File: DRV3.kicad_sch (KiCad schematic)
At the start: 15 parts

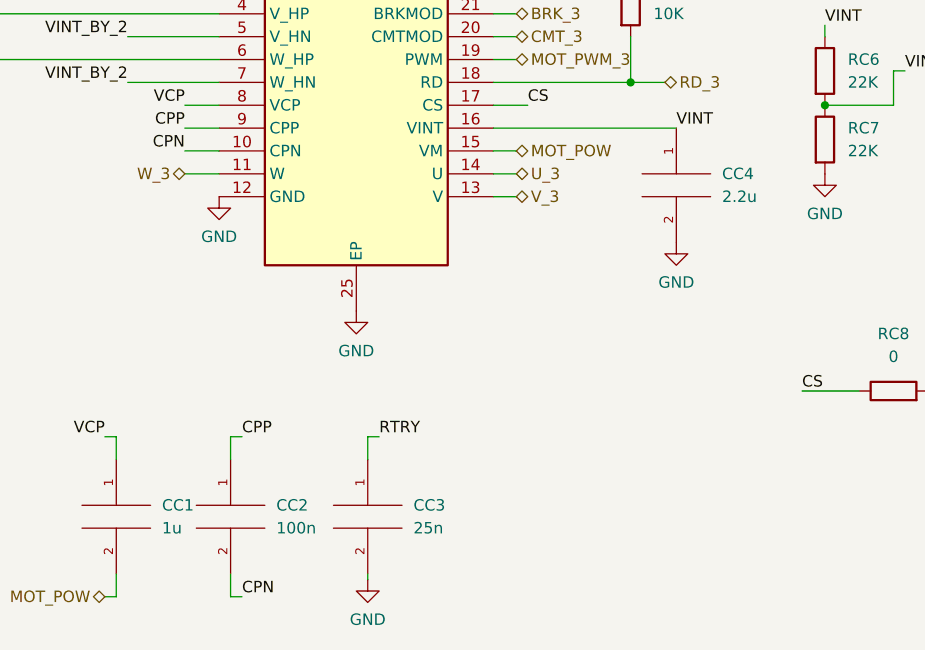
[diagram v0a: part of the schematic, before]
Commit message: MCU circuitry forgot LOL
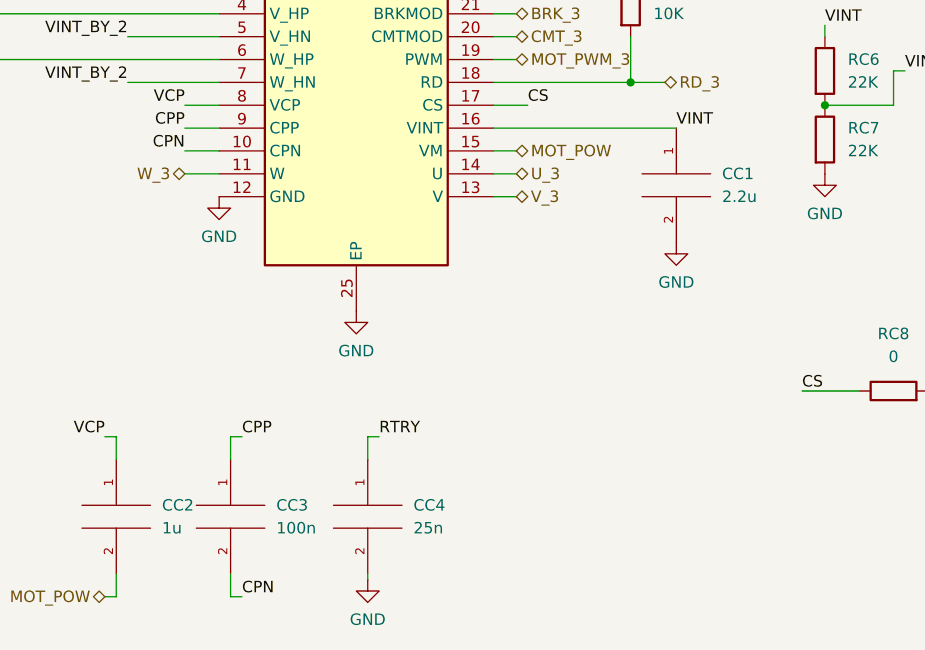
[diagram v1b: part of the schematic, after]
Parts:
- renumbered CC4 to CC1, CC1 to CC2, CC2 to CC3, CC3 to CC4
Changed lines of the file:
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@@
   (symbol (lib_id "upsat-comms-hardware:GND") (at 181.61 109.22 0) (unit 1)
     (in_bom yes) (on_board yes) (fields_autoplaced)
-    (property "Reference" "#PWR0108" (id 0) (at 181.61 115.57 0)
+    (property "Reference" "#PWR0114" (id 0) (at 181.61 115.57 0)
       (effects (font (size 1.27 1.27)) hide)
     )
@@
   (symbol (lib_id "upsat-comms-hardware:GND") (at 130.81 104.14 0) (unit 1)
     (in_bom yes) (on_board yes) (fields_autoplaced)
-    (property "Reference" "#PWR0105" (id 0) (at 130.81 110.49 0)
+    (property "Reference" "#PWR0113" (id 0) (at 130.81 110.49 0)
       (effects (font (size 1.27 1.27)) hide)
     )
@@
   (symbol (lib_id "pspice:C") (at 132.08 139.7 0) (unit 1)
     (in_bom yes) (on_board yes) (fields_autoplaced)
-    (property "Reference" "CC2" (id 0) (at 137.16 138.4299 0)
+    (property "Reference" "CC3" (id 0) (at 137.16 138.4299 0)
       (effects (font (size 1.27 1.27)) (justify left))
     )
@@
   (symbol (lib_id "upsat-comms-hardware:GND") (at 215.9 139.7 0) (unit 1)
     (in_bom yes) (on_board yes) (fields_autoplaced)
-    (property "Reference" "#PWR0110" (id 0) (at 215.9 146.05 0)
+    (property "Reference" "#PWR0116" (id 0) (at 215.9 146.05 0)
       (effects (font (size 1.27 1.27)) hide)
     )
@@
   (symbol (lib_id "pspice:C") (at 147.32 139.7 0) (unit 1)
     (in_bom yes) (on_board yes) (fields_autoplaced)
-    (property "Reference" "CC3" (id 0) (at 152.4 138.4299 0)
+    (property "Reference" "CC4" (id 0) (at 152.4 138.4299 0)
       (effects (font (size 1.27 1.27)) (justify left))
     )
@@
   (symbol (lib_id "pspice:C") (at 119.38 139.7 0) (unit 1)
     (in_bom yes) (on_board yes) (fields_autoplaced)
-    (property "Reference" "CC1" (id 0) (at 124.46 138.4299 0)
+    (property "Reference" "CC2" (id 0) (at 124.46 138.4299 0)
       (effects (font (size 1.27 1.27)) (justify left))
     )
@@
   (symbol (lib_id "upsat-comms-hardware:GND") (at 146.05 116.84 0) (unit 1)
     (in_bom yes) (on_board yes) (fields_autoplaced)
-    (property "Reference" "#PWR0106" (id 0) (at 146.05 123.19 0)
+    (property "Reference" "#PWR0115" (id 0) (at 146.05 123.19 0)
       (effects (font (size 1.27 1.27)) hide)
     )
@@
   (symbol (lib_id "upsat-comms-hardware:GND") (at 198.12 101.6 0) (unit 1)
     (in_bom yes) (on_board yes) (fields_autoplaced)
-    (property "Reference" "#PWR0109" (id 0) (at 198.12 107.95 0)
+    (property "Reference" "#PWR0112" (id 0) (at 198.12 107.95 0)
       (effects (font (size 1.27 1.27)) hide)
     )
@@
   (symbol (lib_id "upsat-comms-hardware:GND") (at 147.32 146.685 0) (unit 1)
     (in_bom yes) (on_board yes) (fields_autoplaced)
-    (property "Reference" "#PWR0107" (id 0) (at 147.32 153.035 0)
+    (property "Reference" "#PWR0117" (id 0) (at 147.32 153.035 0)
       (effects (font (size 1.27 1.27)) hide)
     )
@@
   (symbol (lib_id "pspice:C") (at 181.61 102.87 0) (unit 1)
     (in_bom yes) (on_board yes) (fields_autoplaced)
-    (property "Reference" "CC4" (id 0) (at 186.69 101.5999 0)
-      (effects (font (size 1.27 1.27)) (justify left))
-    )
+    (property "Reference" "CC1" (id 0) (at 186.69 101.5999 0)
+      (effects (font (size 1.27 1.27)) (justify left))
+    )

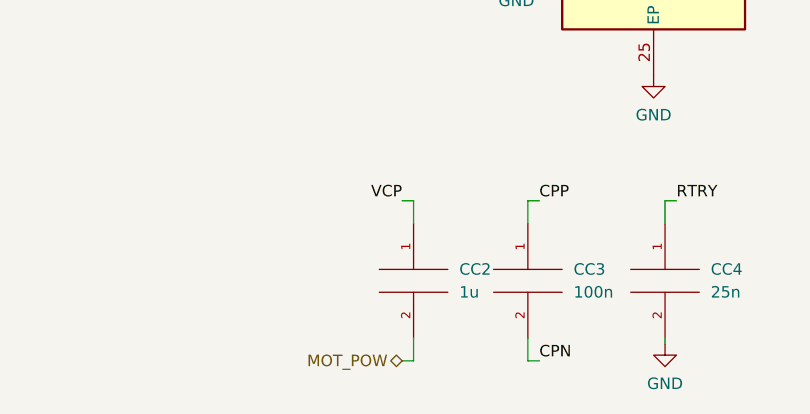
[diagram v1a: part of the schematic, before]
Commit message: All frequency sensitive caps and specific inductor PNs added
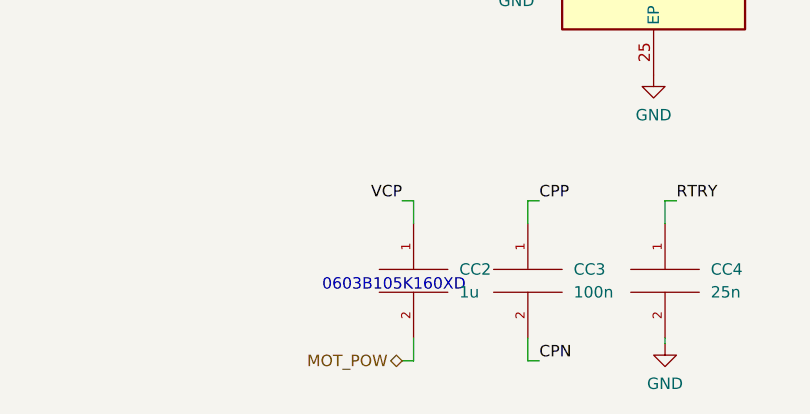
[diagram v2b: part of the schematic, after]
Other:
- note added: "0603B105K160XD"
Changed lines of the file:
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@@
     (stroke (width 0) (type default) (color 0 0 0 0))
+  )
+  (text "0603B105K160XD" (at 109.22 140.97 0)
+    (effects (font (size 1.27 1.27)) (justify left bottom))
   )
   (text "A low-ESR ceramic capacitor must be placed in between the VM and VCP pins. TI recommends a value of 1-µF\nrated for 16 V. Place this component as close as possible to the pins."
